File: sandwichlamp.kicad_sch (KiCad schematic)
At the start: 8 parts, among them J1 Conn_01x01_Pin, J2 Conn_01x01_Pin, J3 Conn_01x01_Pin, J4 12V Enable, U1 magnetic-charger, U2 esp32-wemos-d1-mini, U3 hw357

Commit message: Update PCB
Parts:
- added SW1: SW_SPDT, Connector_PinHeader_2.54mm:PinHeader_1x03_P2.54mm_Vertical, symbol Switch:SW_SPDT
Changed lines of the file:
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@@
+	)
+	(symbol
+		(lib_id "Switch:SW_SPDT")
+		(at 49.53 93.98 0)
+		(unit 1)
+		(exclude_from_sim no)
+		(in_bom yes)
+		(on_board yes)
+		(dnp no)
+		(fields_autoplaced yes)
+		(property "Reference" "SW1"
+			(at 49.53 85.09 0)
+			(effects
+				(font
+					(size 1.27 1.27)
+				)
+			)
+		)
+		(property "Value" "SW_SPDT"
+			(at 49.53 87.63 0)
+			(effects
+				(font
+					(size 1.27 1.27)
+				)
+			)
+		)
+		(property "Footprint" "Connector_PinHeader_2.54mm:PinHeader_1x03_P2.54mm_Vertical"
+			(at 49.53 93.98 0)
+			(effects
+				(font
+					(size 1.27 1.27)
+				)
+				(hide yes)
+			)
+		)
+		(property "Datasheet" "~"
+			(at 49.53 101.6 0)
+			(effects
+				(font
+					(size 1.27 1.27)
+				)
+				(hide yes)
+			)
+		)
+		(property "Description" "Switch, single pole double throw"
+			(at 49.53 93.98 0)
+			(effects
+				(font
+					(size 1.27 1.27)
+				)
+				(hide yes)
+			)
+		)
+		(pin "3"
+		)
+		(pin "2"
+		)
+		(pin "1"
+		)
+		(instances
+			(project ""
+				(path "/e0ec050d-3d79-41e4-bfa7-38c68df5e8aa"
+					(reference "SW1")
+					(unit 1)
+				)
+			)
+		)
 	)
 	(symbol

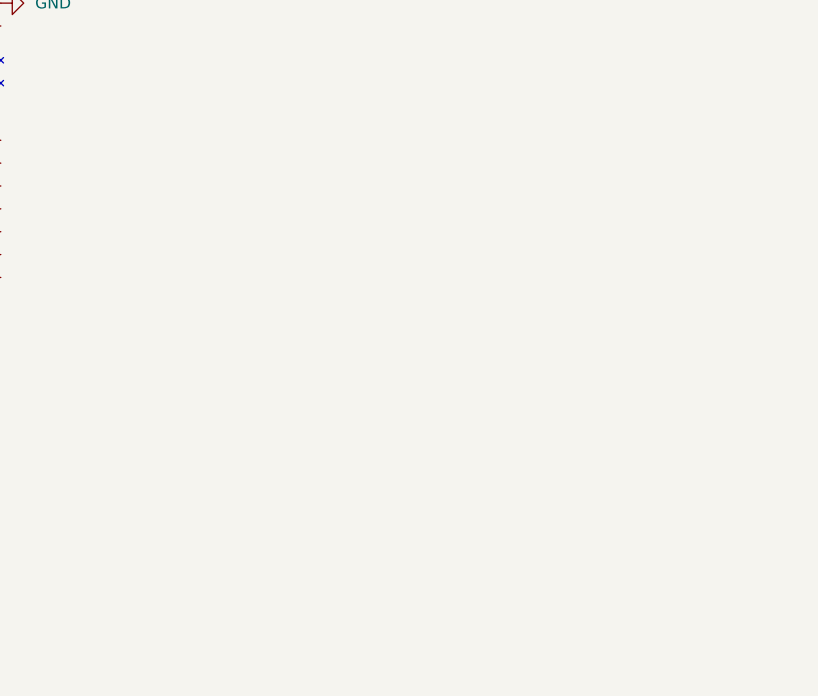
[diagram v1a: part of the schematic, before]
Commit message: Add radar sensor
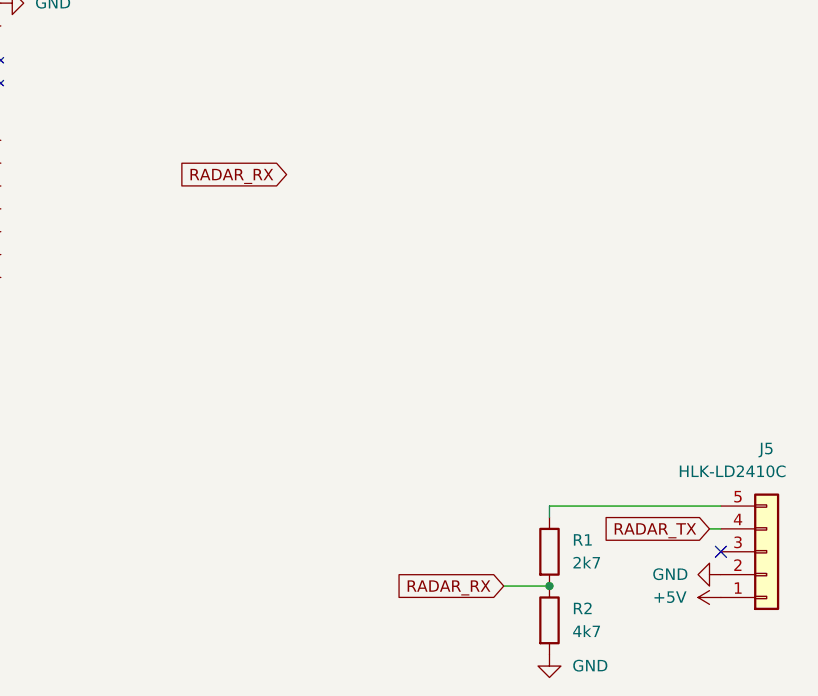
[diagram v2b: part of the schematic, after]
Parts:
- added J5: HLK-LD2410C, Connector_PinHeader_2.54mm:PinHeader_1x05_P2.54mm_Vertical, symbol Connector_Generic:Conn_01x05
- added R1: 2k7, Resistor_THT:R_Axial_DIN0207_L6.3mm_D2.5mm_P7.62mm_Horizontal, symbol Device:R
- added R2: 4k7, Resistor_THT:R_Axial_DIN0207_L6.3mm_D2.5mm_P7.62mm_Horizontal, symbol Device:R
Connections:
- net +5V: now also J5.1 (Pin_1)
- net GND: now also J5.2 (Pin_2), R2.2
- new net: J5.5 (Pin_5), R1.1
- new net RADAR_RX: R1.2, R2.1
- new net RADAR_TX: J5.4 (Pin_4)
- no-connect marks 0 -> 1

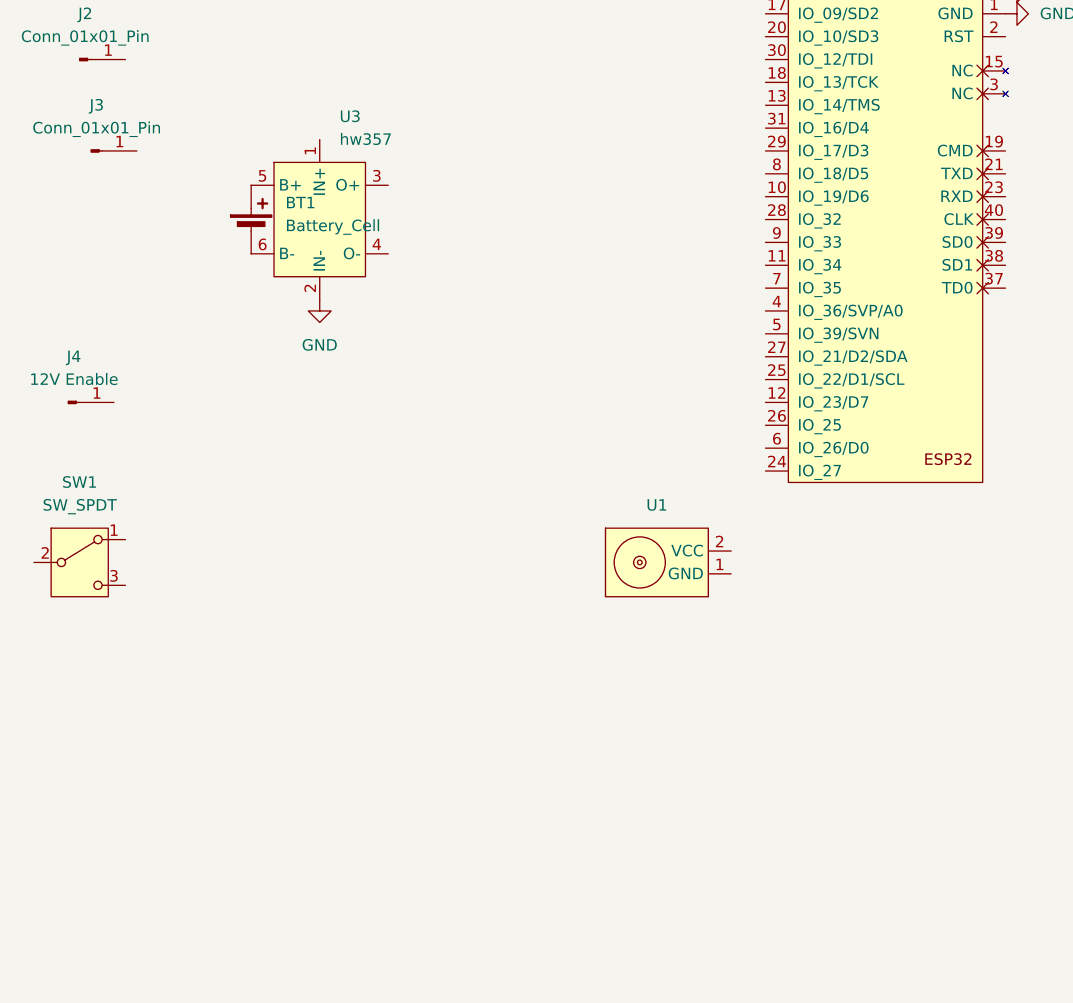
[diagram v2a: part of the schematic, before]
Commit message: Add BME280 and radio-receiver and continue with the placement of the components
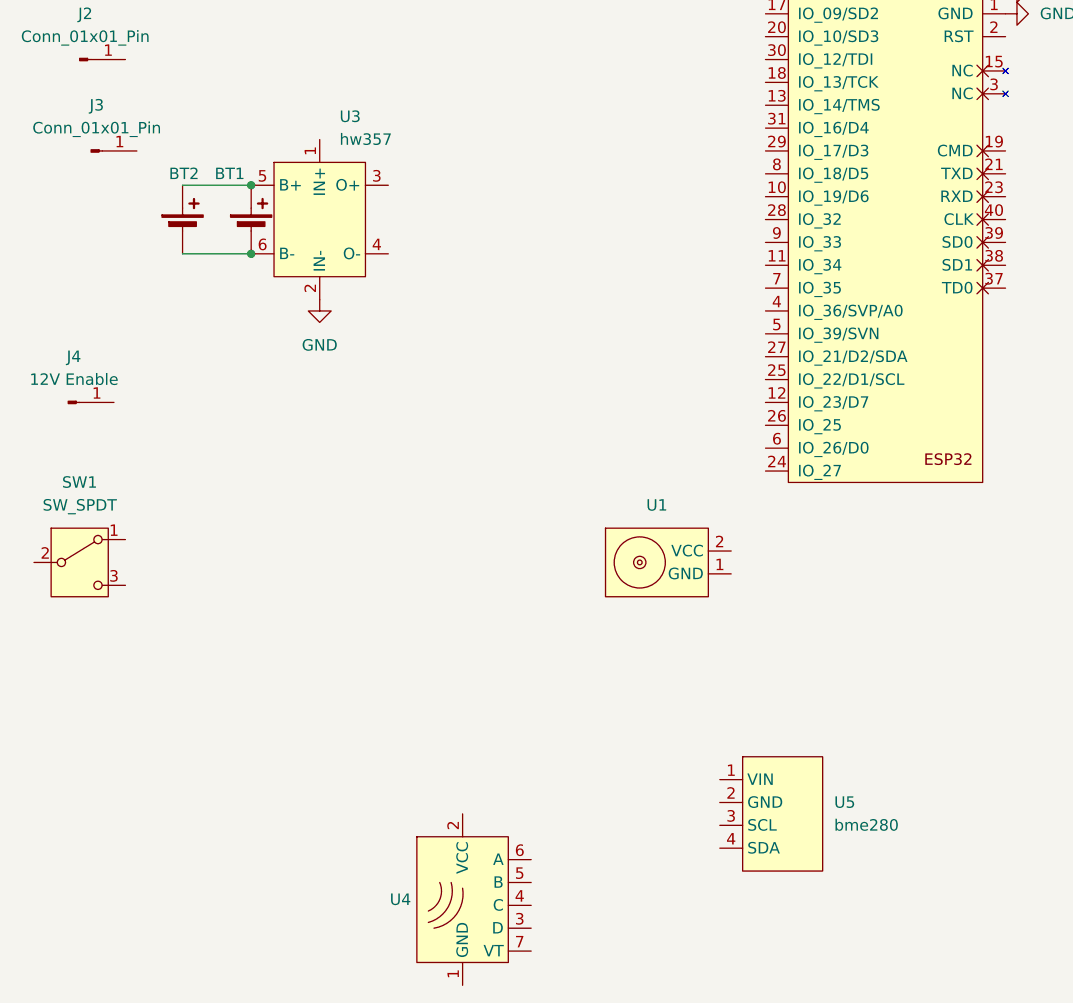
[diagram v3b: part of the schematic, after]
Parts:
- added BT2: Battery_Cell, Connector_JST:JST_PH_B2B-PH-K_1x02_P2.00mm_Vertical, symbol Device:Battery_Cell
- added U4: RX480E, radio-receiver:radio-receiver, symbol radio-receiver:radio-receiver
- added U5: bme280, bme280:bme280, symbol bme280:bme280
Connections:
- net at BT1.1 (+), U3.5 (B+): now also BT2.1 (+)
- net at BT1.2 (-), U3.6 (B-): now also BT2.2 (-)

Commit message: Add new esp footprint
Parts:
- added D2: D_Small, symbol Device:D_Small
- added J6: Conn_01x20_Pin, Connector_PinHeader_2.54mm:PinHeader_1x20_P2.54mm_Vertical, symbol Connector:Conn_01x20_Pin
- added U6: DS18B20, Package_TO_SOT_THT:TO-92L_Inline_Wide, symbol Sensor_Temperature:DS18B20
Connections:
- net +5V: no longer U2.35 (VCC_(USB))
- net GND: now also BT1.2 (-), BT2.2 (-), U3.4 (O-), U3.6 (B-)
- net +4V: now reaches BT1.1 (+), BT2.1 (+), U3.5 (B+)
- net +4V: now also D2.2 (A)
- net VBUS: now reaches U3.1 (IN+)
- net VBUS: now also SW1.2 (B), U2.35 (VCC_(USB))
- net +12V: now reaches U3.3 (O+)
- net at SW1.3 (C): now also D2.1 (K)
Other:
- note added: "In case there is no USB 5V then the battery will power the ESP"
- moved on the sheet: J1, J2, J3, SW1
